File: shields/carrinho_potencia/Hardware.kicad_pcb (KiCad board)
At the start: 2 copper layers, 135.8 x 56.1 mm, 87 parts, among them J1 Conn_01x02, J10 Conn_01x04, J11 Conn_01x04, J12 Conn_02x13_Odd_Even, J13 Conn_01x02, J14 Conn_01x02, J2 Conn_01x04, J3 Conn_01x02, J4 Conn_01x02_Male, J5 Conn_01x02_Male, J6 Conn_01x02_Male, J7 Conn_01x02_Male, J8 Conn_01x03, J9 Conn_01x03, Q1 BD140, Q10 BC548, Q11 BD139, Q12 BD139, Q2 BD140, Q3 BC548, Q4 BC548, Q5 BD139, Q6 BD139, Q7 BD140, Q8 BD140, Q9 BC548, U1 LM393, U2 TCRT5000, U3 LM324, U4 HC-05, U5 TCRT5000

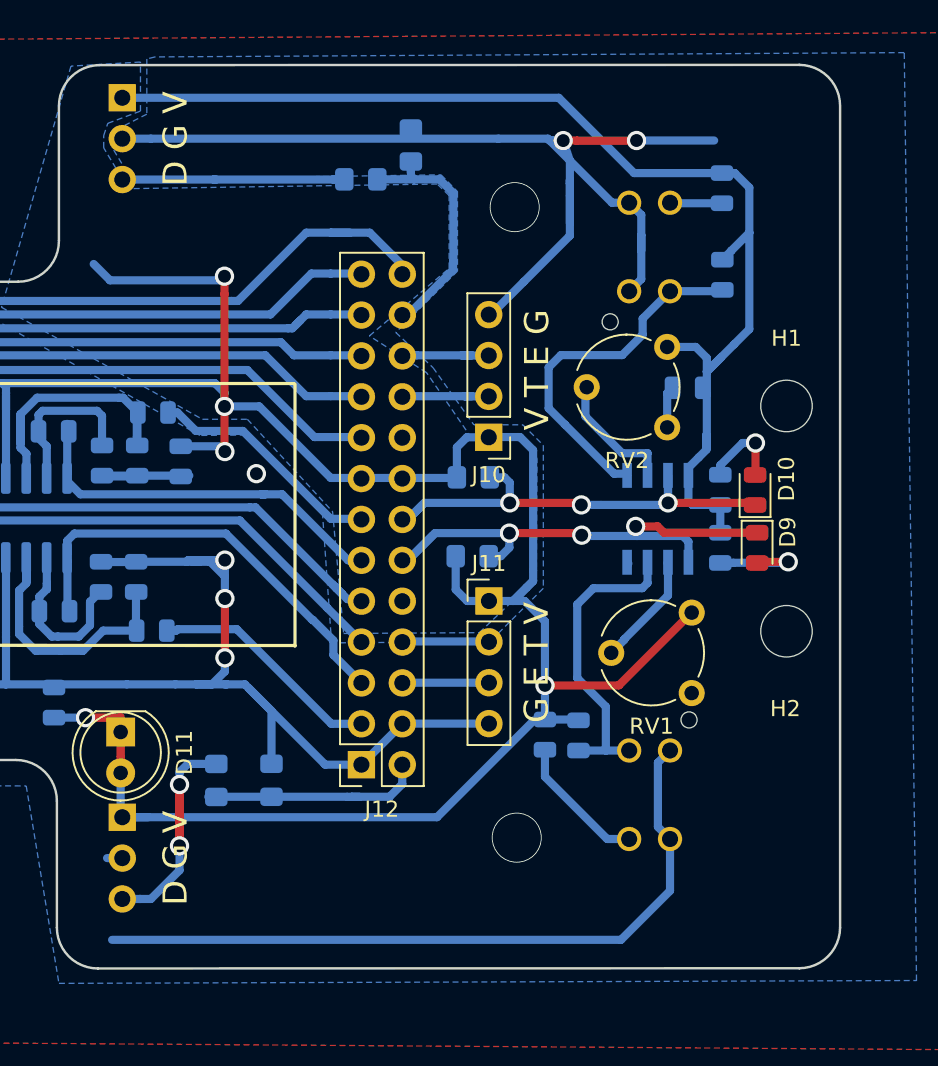
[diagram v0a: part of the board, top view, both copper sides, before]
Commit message: Added 3d model
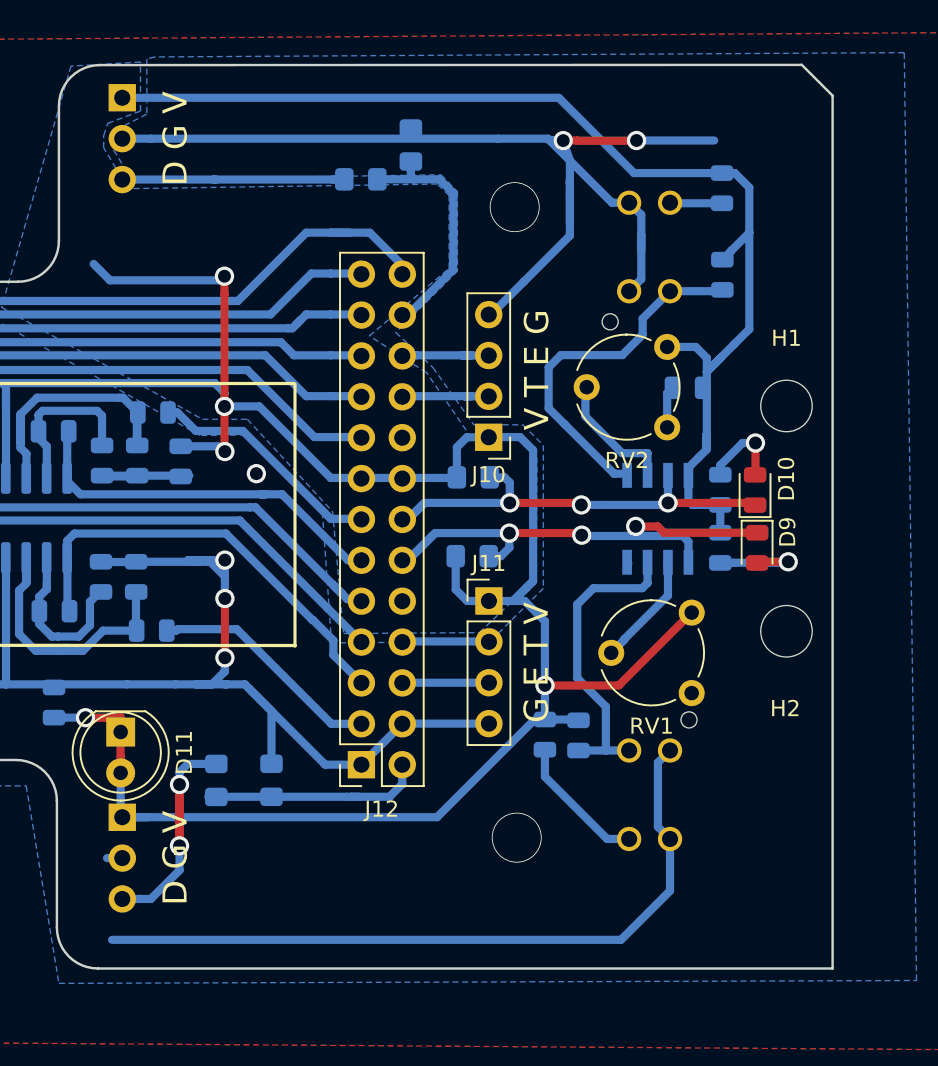
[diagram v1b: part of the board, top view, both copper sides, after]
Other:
- board size 135.8 x 56.1 mm -> 135.3 x 56.2 mm
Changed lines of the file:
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@@
   (general
     (thickness 1.6)
-    (drawings 42)
+    (drawings 41)
     (tracks 936)
     (zones 0)
@@
     )
   )
-  (gr_line (start 266.0142 34.3154) (end 266.0142 85.3694) (layer Edge.Cuts) (width 0.15))
+  (gr_line (start 265.55 33.66) (end 263.63 31.74) (layer Edge.Cuts) (width 0.15))
+  (gr_line (start 265.55 87.9) (end 265.55 33.66) (layer Edge.Cuts) (width 0.15))
+  (gr_line (start 219.9 87.9) (end 265.55 87.9) (layer Edge.Cuts) (width 0.15))
+  (gr_line (start 217.3478 77.4827) (end 217.3478 85.3567) (layer Edge.Cuts) (width 0.15))
+  (gr_arc (start 219.8878 85.3567) (end 217.3478 85.3567) (angle -90) (layer Edge.Cuts) (width 0.15))
+  (gr_arc (start 214.8078 77.4827) (end 217.3478 77.4827) (angle -90) (layer Edge.Cuts) (width 0.15))
   (gr_arc (start 220.0148 34.3027) (end 220.0148 31.7627) (angle -90) (layer Edge.Cuts) (width 0.15))
   (gr_text "D G V\n" (at 224.7138 36.3347 90) (layer F.SilkS)
@@
   (gr_arc (start 165.0238 43.7007) (end 163.4998 43.7007) (angle -90) (layer Edge.Cuts) (width 0.15))
   (gr_line (start 163.4998 77.6097) (end 163.4998 76.4667) (layer Edge.Cuts) (width 0.2))
-  (gr_arc (start 219.8878 85.3567) (end 217.3478 85.3567) (angle -90) (layer Edge.Cuts) (width 0.15))
   (gr_arc (start 161.9758 77.6097) (end 161.9758 79.1337) (angle -90) (layer Edge.Cuts) (width 0.15))
   (gr_line (start 165.0238 74.9427) (end 214.8078 74.9427) (layer Edge.Cuts) (width 0.15))
-  (gr_line (start 217.3478 77.4827) (end 217.3478 85.3567) (layer Edge.Cuts) (width 0.15))
   (gr_arc (start 214.9348 42.6847) (end 214.9348 45.2247) (angle -90) (layer Edge.Cuts) (width 0.15))
   (gr_line (start 194.0433 51.5493) (end 232.0671 51.5493) (layer F.SilkS) (width 0.2))
@@
   (gr_arc (start 132.7658 43.5737) (end 132.7658 41.0337) (angle -90) (layer Edge.Cuts) (width 0.15))
   (gr_line (start 232.1433 51.5874) (end 232.1433 67.8688) (layer F.SilkS) (width 0.2))
-  (gr_arc (start 214.8078 77.4827) (end 217.3478 77.4827) (angle -90) (layer Edge.Cuts) (width 0.15))
   (gr_line (start 232.1433 67.8307) (end 194.1703 67.8053) (layer F.SilkS) (width 0.2))
   (gr_line (start 132.7658 79.1337) (end 161.9758 79.1337) (layer Edge.Cuts) (width 0.15))
@@
   (gr_line (start 193.675 50.7873) (end 193.675 68.5673) (layer F.SilkS) (width 0.2))
   (gr_line (start 194.0941 67.7926) (end 194.0433 51.5366) (layer F.SilkS) (width 0.2))
-  (gr_arc (start 263.4742 85.344) (end 263.4742 87.884) (angle -90) (layer Edge.Cuts) (width 0.15))
-  (gr_line (start 219.8878 87.8967) (end 263.4996 87.884) (layer Edge.Cuts) (width 0.15))
-  (gr_line (start 220.0148 31.7627) (end 263.4996 31.75) (layer Edge.Cuts) (width 0.15))
-  (gr_arc (start 263.4742 34.29) (end 266.0142 34.29) (angle -90) (layer Edge.Cuts) (width 0.15))
+  (gr_line (start 220.0148 31.7627) (end 263.64 31.75) (layer Edge.Cuts) (width 0.15))
   (via (at 245.7958 40.5892) (size 3.1) (drill 3) (layers F.Cu B.Cu) (net 0))
   (via (at 245.9228 79.7687) (size 3.1) (drill 3) (layers F.Cu B.Cu) (net 0))
@@
   (segment (start 161.3408 64.6176) (end 161.3408 64.516) (width 0.508) (layer B.Cu) (net 16))
   (segment (start 161.3408 64.516) (end 162.0901 63.7667) (width 0.708) (layer B.Cu) (net 16))
+  (segment (start 167.64 63.7667) (end 167.64 68.462) (width 0.508) (layer B.Cu) (net 16))
   (segment (start 149.646355 64.194475) (end 150.352264 64.900384) (width 0.708) (layer B.Cu) (net 17))
   (segment (start 149.562355 64.194475) (end 149.646355 64.194475) (width 0.708) (layer B.Cu) (net 17))
@@
   (segment (start 221.264 72.3138) (end 221.3102 72.2676) (width 0.508) (layer F.Cu) (net 67))
   (segment (start 219.1258 72.3138) (end 221.264 72.3138) (width 0.508) (layer F.Cu) (net 67))
-  (segment (start 167.64 63.7667) (end 167.64 68.462) (width 0.508) (layer B.Cu) (net 16))
   (zone (net 16) (net_name +BATT) (layer B.Cu) (hatch edge 0.508)
     (connect_pads (clearance 0.3048))
@@
     )
   )
-  (zone (net 2) (net_name +5V) (layer B.Cu) (hatch edge 0.508)
+  (zone (net 1) (net_name GND) (layer F.Cu) (hatch edge 0.508)
     (connect_pads (clearance 0.3048))
     (min_thickness 0.254)
@@
     (polygon
       (pts
-        (xy 226.3902 53.7718) (xy 229.1842 53.7718) (xy 234.4801 59.5122) (xy 235.1659 67.0814) (xy 243.5987 67.0306)
-        (xy 247.142 63.6524) (xy 247.1801 56.2102) (xy 246.4181 54.9402) (xy 243.1161 54.9402) (xy 240.3221 50.8762)
-        (xy 236.7661 48.5902) (xy 241.7191 44.3992) (xy 241.7191 39.8653) (xy 240.9825 39.1541) (xy 221.5261 39.4462)
-        (xy 221.0181 38.1762) (xy 220.2561 36.9062) (xy 220.2561 36.1442) (xy 220.5101 35.3822) (xy 222.5421 34.6202)
-        (xy 222.5421 31.5722) (xy 218.2241 31.8262) (xy 213.9061 46.8122)
+        (xy 129.032 30.734) (xy 276.606 29.718) (xy 275.844 92.964) (xy 128.778 91.948) (xy 127 80.772)
       )
     )
@@
     )
   )
-  (zone (net 1) (net_name GND) (layer F.Cu) (hatch edge 0.508)
+  (zone (net 2) (net_name +5V) (layer B.Cu) (hatch edge 0.508)
     (connect_pads (clearance 0.3048))
     (min_thickness 0.254)
@@
     (polygon
       (pts
-        (xy 129.032 30.734) (xy 276.606 29.718) (xy 275.844 92.964) (xy 128.778 91.948) (xy 127 80.772)
+        (xy 226.3902 53.7718) (xy 229.1842 53.7718) (xy 234.4801 59.5122) (xy 235.1659 67.0814) (xy 243.5987 67.0306)
+        (xy 247.142 63.6524) (xy 247.1801 56.2102) (xy 246.4181 54.9402) (xy 243.1161 54.9402) (xy 240.3221 50.8762)
+        (xy 236.7661 48.5902) (xy 241.7191 44.3992) (xy 241.7191 39.8653) (xy 240.9825 39.1541) (xy 221.5261 39.4462)
+        (xy 221.0181 38.1762) (xy 220.2561 36.9062) (xy 220.2561 36.1442) (xy 220.5101 35.3822) (xy 222.5421 34.6202)
+        (xy 222.5421 31.5722) (xy 218.2241 31.8262) (xy 213.9061 46.8122)
       )
     )

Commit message: Removed backup files
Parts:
- D11: footprint LED_THT:LED_D5.0mm -> LED_SMD:LED_0805_2012Metric
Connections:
- D12 pad 1: Net-(D12-Pad1) -> +BATT
- D12 pad 2: +BATT -> Net-(D12-Pad2)
- J2 pad 1: +BATT -> Net-(D12-Pad2)
- J6 pad 1: Net-(D12-Pad1) -> +BATT
- J6 pad 2: Net-(D12-Pad1) -> +BATT
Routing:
- net Net-(D12-Pad2): track 0.00 -> 4.70 mm
- net +BATT: track 181.5 -> 176.8 mm
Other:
- board size 135.3 x 56.2 mm -> 135.8 x 56.1 mm
